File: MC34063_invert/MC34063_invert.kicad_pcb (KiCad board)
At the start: 2 copper layers, 88.6 x 23 mm, 23 parts, among them J1 INPUT, J2 OUTPUT, Q1 2N2907, U1 MC34063AP

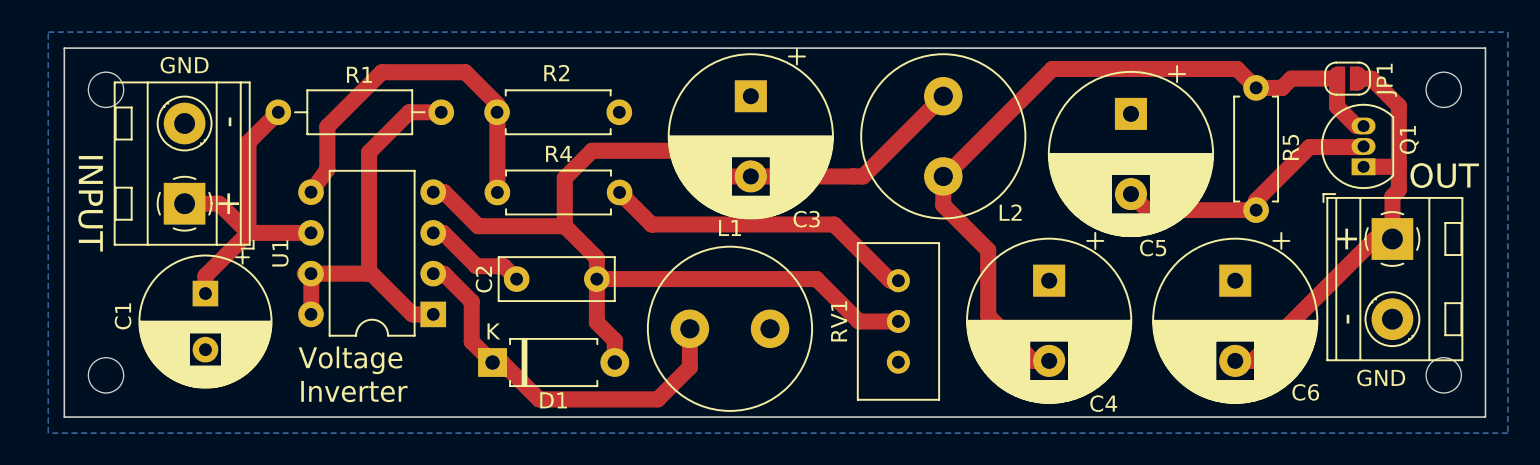
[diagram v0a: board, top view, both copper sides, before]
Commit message: Simplified Inverter
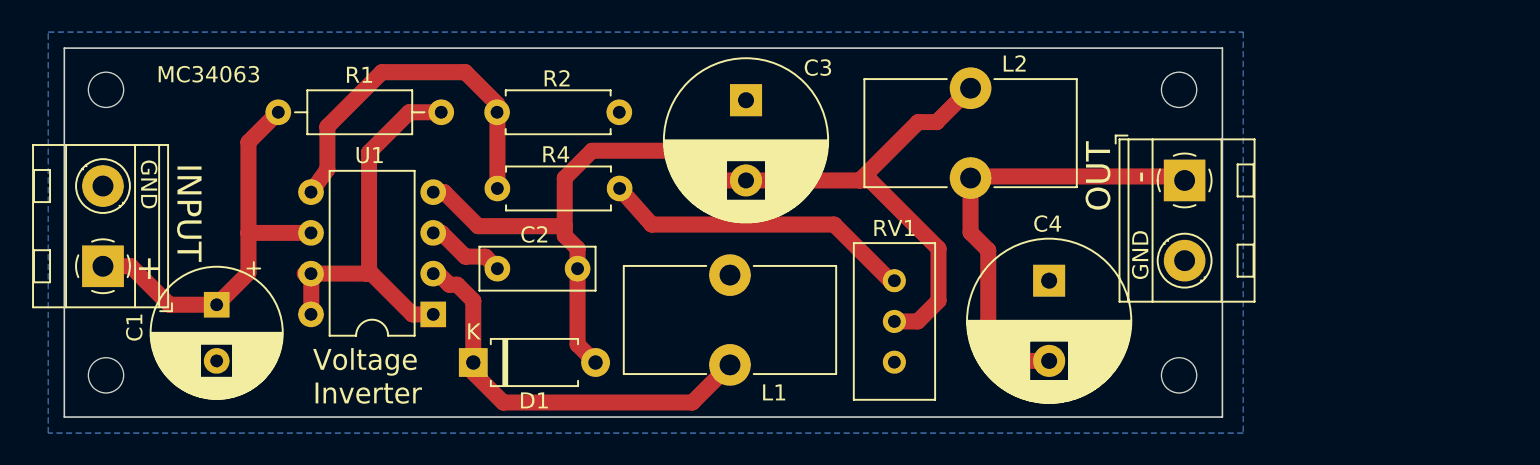
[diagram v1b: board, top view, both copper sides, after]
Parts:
- removed C5, C6: 470u, Capacitor_THT:CP_Radial_D10.0mm_P5.00mm
- removed JP1: Jumper, Jumper:SolderJumper-2_P1.3mm_Open_RoundedPad1.0x1.5mm
- removed Q1: 2N2907, Package_TO_SOT_THT:TO-92_Inline
- removed R5: 100, Resistor_THT:R_Axial_DIN0207_L6.3mm_D2.5mm_P7.62mm_Horizontal
- C2: value 100p -> 4.7nF
- D1: value 1N5817 -> 1N5819
- L1: value 10u -> 100u; footprint Inductor_THT:L_Radial_D10.0mm_P5.00mm_Neosid_SD12k_style3 -> Inductor_THT:L_Toroid_Vertical_L13.0mm_W6.5mm_P5.60mm
- L2: value 5m -> 470uH; footprint Inductor_THT:L_Radial_D10.0mm_P5.00mm_Neosid_SD12k_style3 -> Inductor_THT:L_Toroid_Vertical_L13.0mm_W6.5mm_P5.60mm
- R2: value 2K2 -> 82K
- moved H3 16.5 mm to (114.5, 61.6)
- moved H4 16.5 mm to (114.5, 79.4)
- moved J2 13.5 mm to (114.8, 67.2)
- moved J1 6.41 mm to (47.4, 72.6)
- moved L1 3.36 mm to (86.5, 78.8), turned to 180 degrees
- moved L2 1.77 mm to (101.5, 61.5), turned to 0 degrees
- moved C2 1.36 mm to (72.0, 72.8)
- moved D1 1.20 mm to (70.5, 78.6)
- moved C1 0.99 mm to (54.5, 75.0)
- moved C3 0.39 mm to (87.5, 62.2)
- moved R4 0.25 mm to (72.0, 67.8)
- moved RV1 0.25 mm to (96.8, 73.5)
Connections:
- C4 pad 2: Net-(C4-Pad2) -> Net-(J2-Pin_1)
- J2 pad 1: Net-(C6-Pad2) -> Net-(J2-Pin_1)
- L2 pad 2: Net-(C4-Pad2) -> Net-(J2-Pin_1)
- RV1 pad 3: (no net) -> unconnected-(RV1-Pad3)
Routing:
- net Net-(C4-Pad2): track 46.8 -> 0.00 mm
- net Net-(J2-Pin_1): track 0.00 -> 28.0 mm
- net Net-(C6-Pad2): track 26.9 -> 0.00 mm
- net Net-(C5-Pad2): track 16.9 -> 0.00 mm
- net Net-(D1-A): track 68.8 -> 63.7 mm
- net Net-(J1-Pin_1): track 21.8 -> 25.7 mm
- net Net-(D1-K): track 23.9 -> 25.4 mm
- net Net-(U1-TC): track 6.39 -> 4.92 mm
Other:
- board size 88.6 x 23 mm -> 72.2 x 23 mm
- net class Default removed
- net class PWR removed
- board text added: "MC34063"
